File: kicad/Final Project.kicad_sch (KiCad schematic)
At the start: 15 parts, among them J1 Mini-DIN-6, SW1 Button, U1 TSOP382xx, U2 ATMEGA328p-u, Y1 Crystal

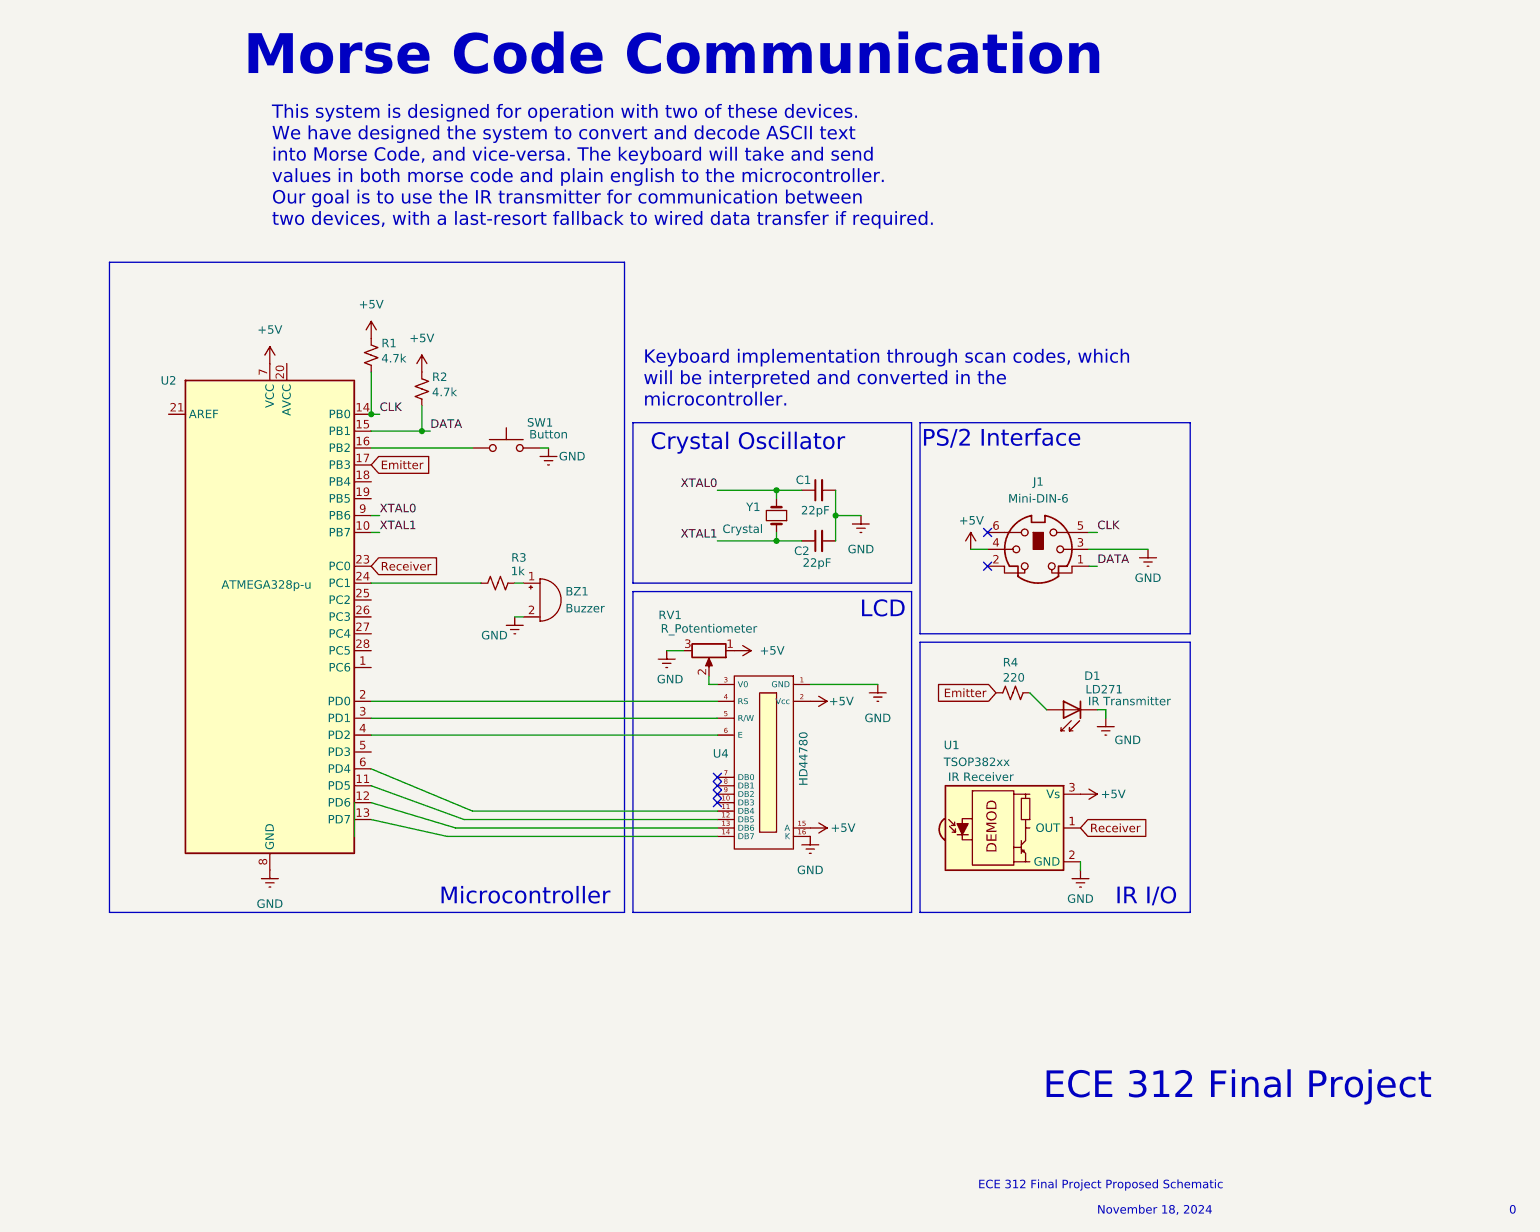
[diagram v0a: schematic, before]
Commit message: removed old plan and start final implementation
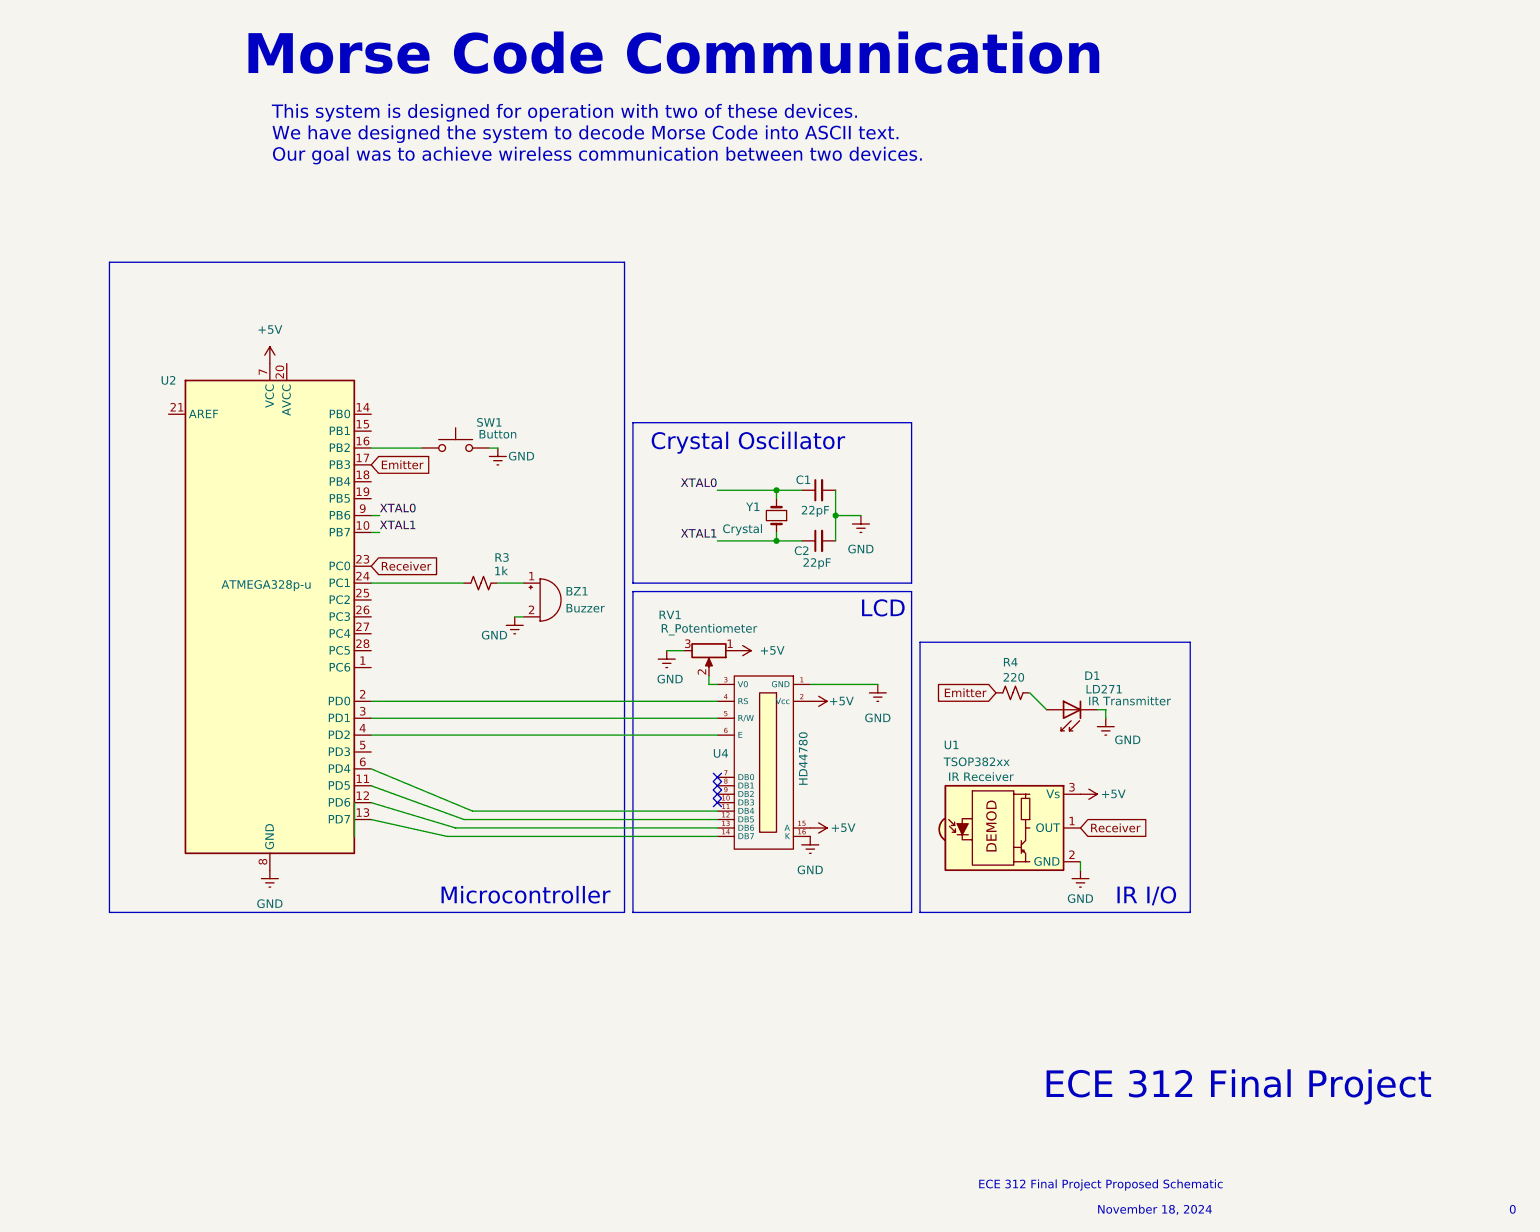
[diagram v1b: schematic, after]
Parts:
- removed J1: Mini-DIN-6, symbol Connector:Mini-DIN-6
- removed R1, R2: 4.7k, symbol Device:R_Small_US
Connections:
- net CLK: no longer names the net of U2.14 (PB0)
- net DATA: no longer names the net of U2.15 (PB1)
- no-connect marks 6 -> 4
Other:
- note removed: "PS/2 Interface"
- moved on the sheet: R3, SW1

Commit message: moved main.c pin configs to header and schematic done
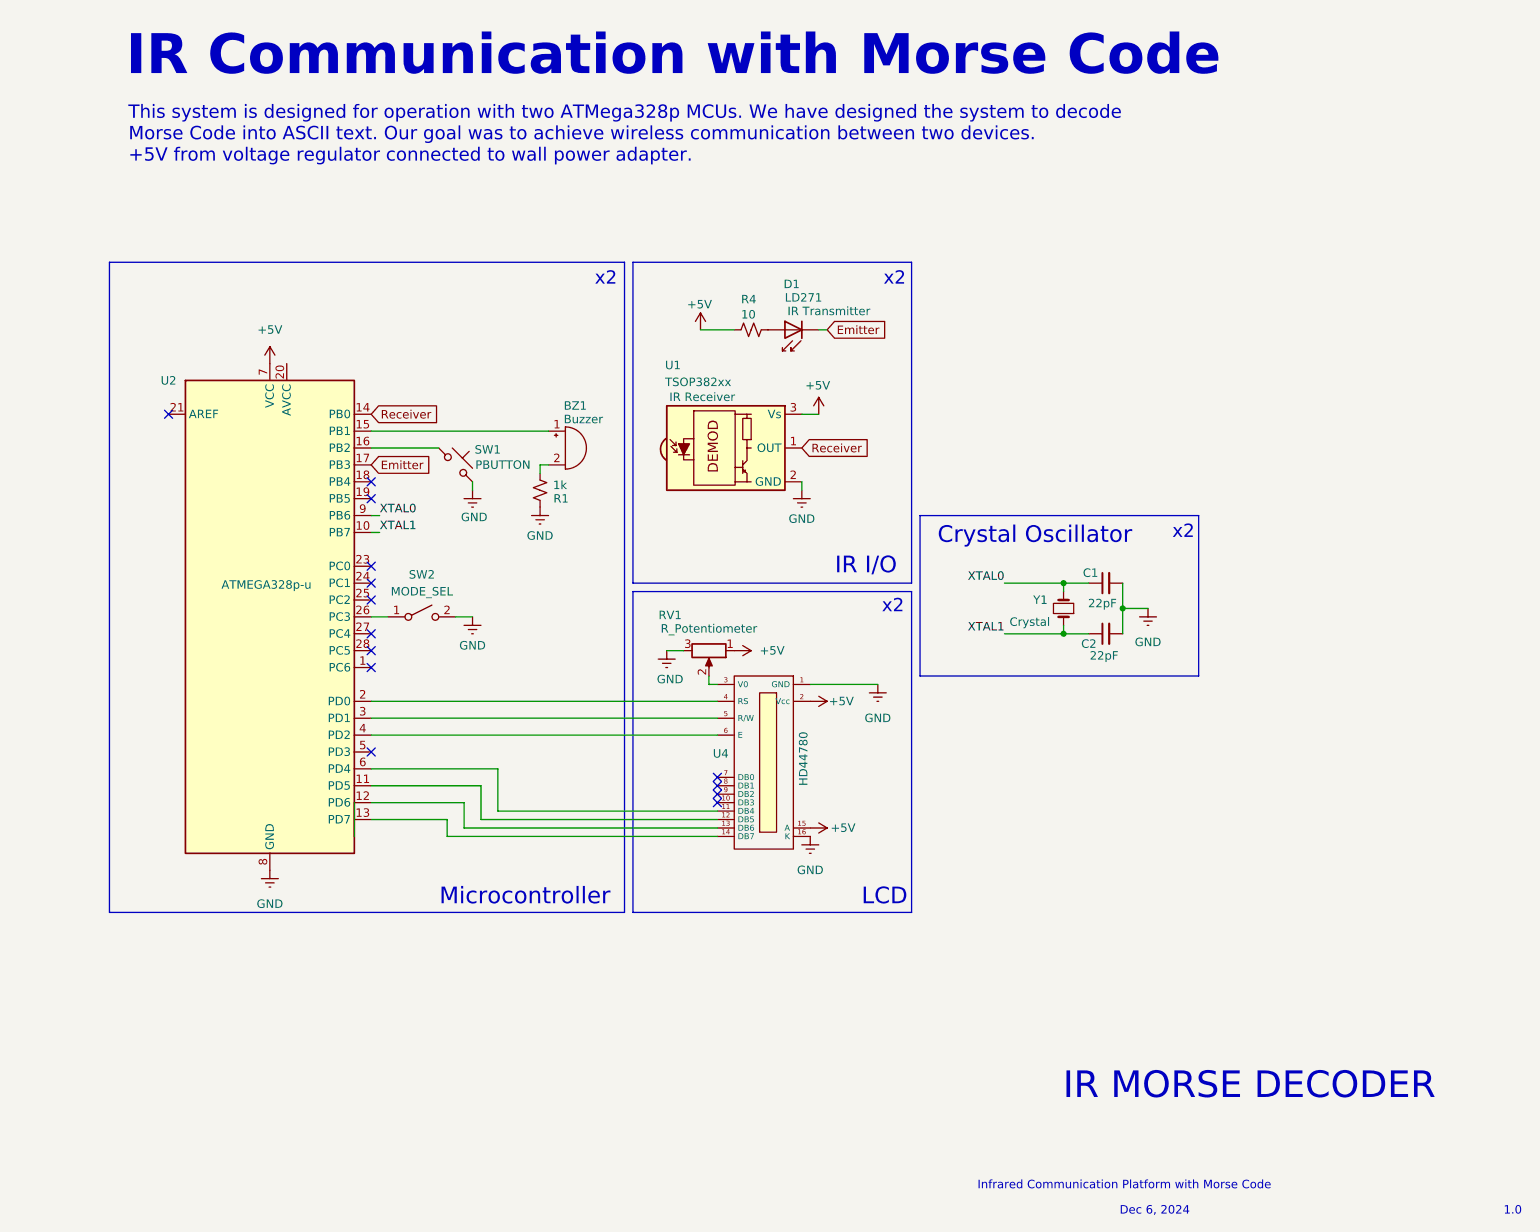
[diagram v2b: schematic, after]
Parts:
- removed R3: 1k, symbol Device:R_Small_US
- removed SW1: Button, symbol Switch:SW_Push
- added R1: 1k, symbol Device:R_Small_US
- added SW1: PBUTTON, symbol Switch:SW_Push_45deg
- added SW2: MODE_SEL, symbol Switch:SW_SPST
- R4: value 220 -> 10
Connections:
- net +5V: now also R4.2
- net Emitter: now also D1.1 (K); no longer R4.2
- net GND: now also R1.1, SW1.2, SW2.2 (B); no longer BZ1.2 (-), D1.1 (K)
- net Receiver: now also U2.14 (PB0); no longer U2.23 (PC0)
- net at BZ1.1 (+): now also U2.15 (PB1)
- net at U2.16 (PB2): now also SW1.1
- net at U2.26 (PC3): now also SW2.1 (A)
- new net: BZ1.2 (-), R1.2
- no-connect marks 4 -> 14
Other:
- note added: "1.0"
- note added: "Dec 6, 2024"
- note added: "IR Communication with Morse Code"
- note added: "IR MORSE DECODER"
- note added: "Infrared Communication Platform with Morse Code"
- note added: "x2"
- note removed: "0"
- note removed: "ECE 312 Final Project"
- note removed: "ECE 312 Final Project Proposed Schematic"
- note removed: "Morse Code Communication"
- note removed: "November 18, 2024"
- moved on the sheet: BZ1, C1, C2, D1, R4, U1, Y1

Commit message: updated schematics
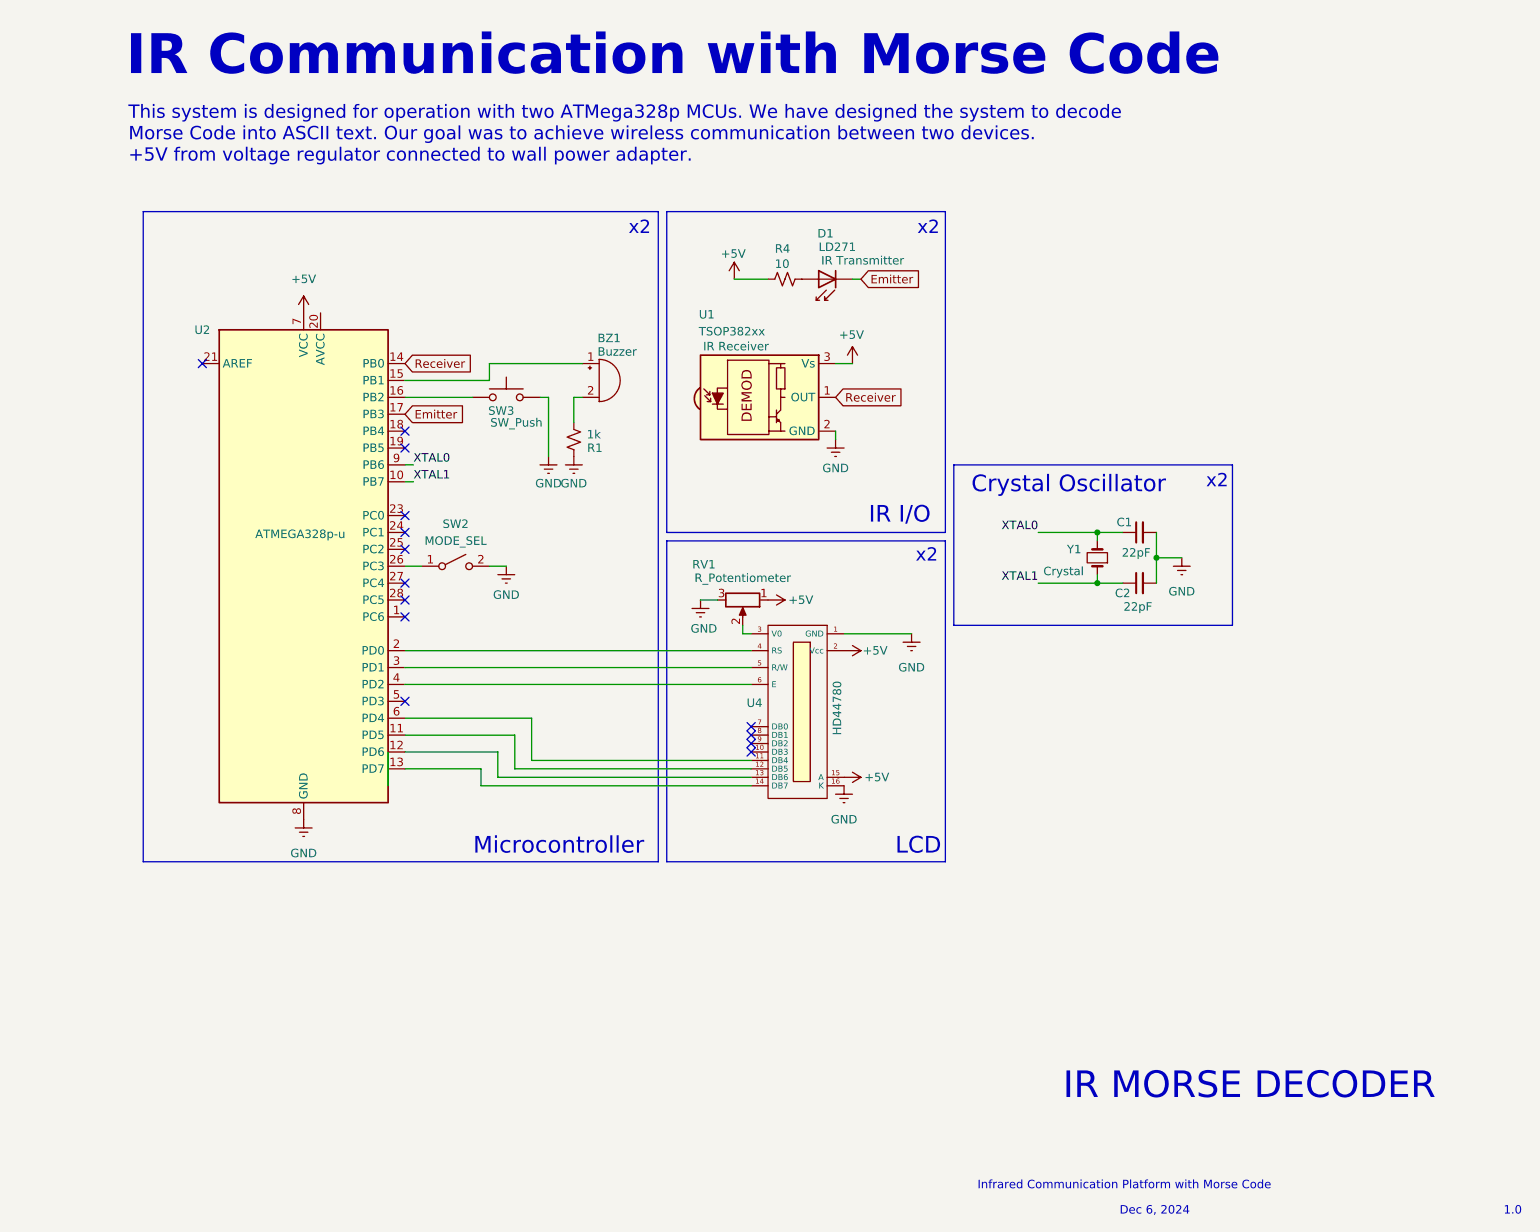
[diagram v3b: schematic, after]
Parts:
- removed SW1: PBUTTON, symbol Switch:SW_Push_45deg
- added SW3: SW_Push, symbol Switch:SW_Push
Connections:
- net GND: now also SW3.2
- net at U2.16 (PB2): now also SW3.1
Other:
- moved on the sheet: BZ1, C1, C2, D1, R1, R4, RV1, SW2, U1, U2, U4, Y1
